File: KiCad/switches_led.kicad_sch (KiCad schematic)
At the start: 70 parts, among them Q2 MMBT3904, Q3 MMBT3904, Q4 MMBT3904, Q5 MMBT3904, Q6 MMBT3904, Q7 MMBT3904, Q8 MMBT3904, Q9 MMBT3904, U3 CD4017BE

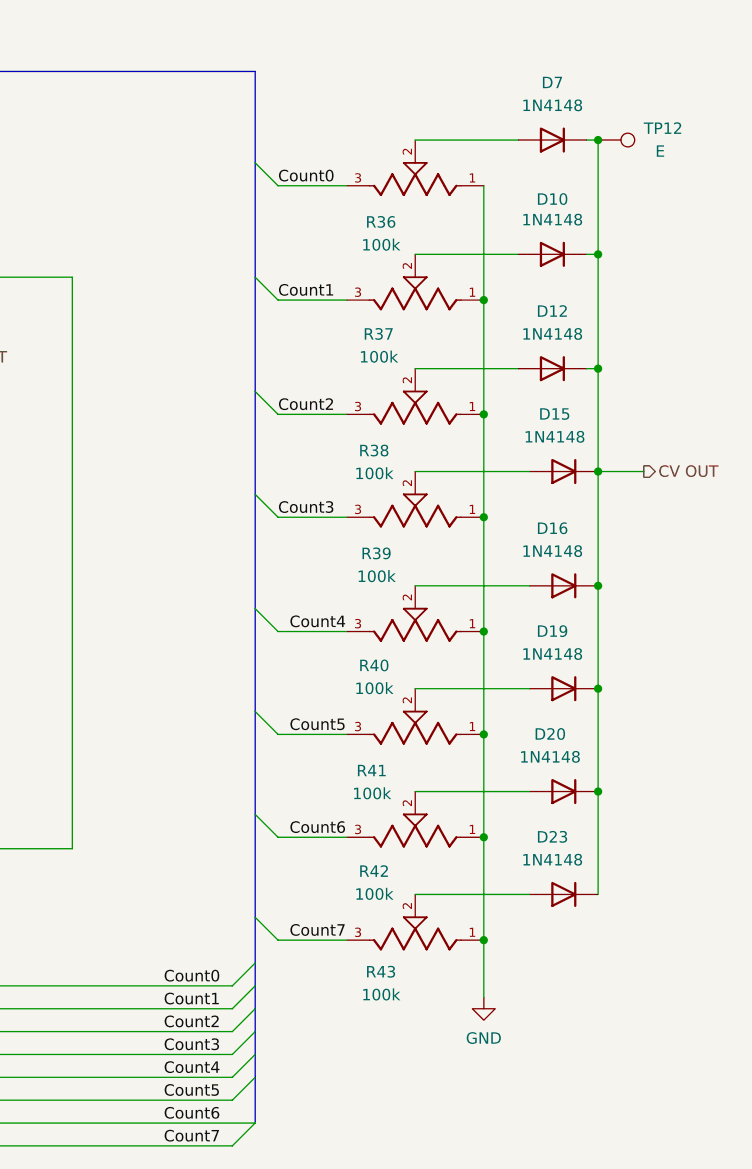
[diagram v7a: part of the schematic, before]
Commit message: fixing drc errors; mirroring potentiometers in sch due to error; mirroring switches on pcb
to do: change symbol description potentiometer (cw, ccw)
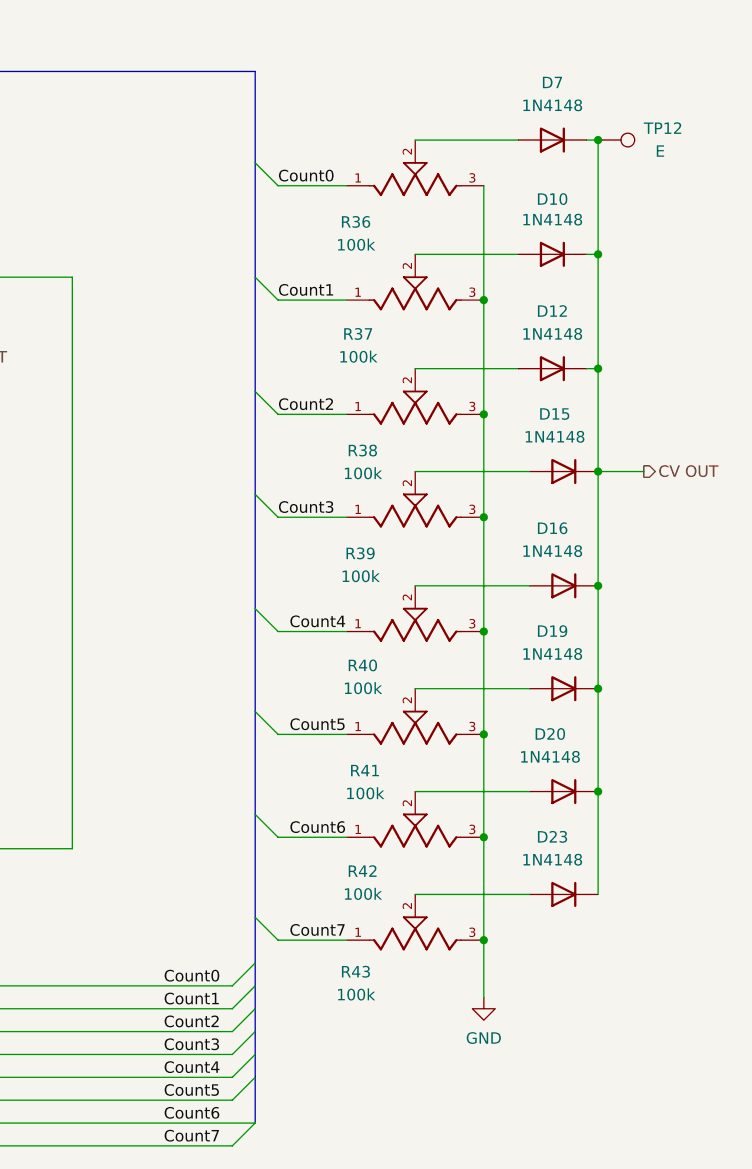
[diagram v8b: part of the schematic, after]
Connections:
- net Count0: now also R36.1; no longer R36.3
- net Count1: now also R37.1; no longer R37.3
- net Count2: now also R38.1; no longer R38.3
- net Count3: now also R39.1; no longer R39.3
- net Count4: now also R40.1; no longer R40.3
- net Count5: now also R41.1; no longer R41.3
- net Count6: now also R42.1; no longer R42.3
- net Count7: now also R43.1; no longer R43.3
- net GND: now also R36.3, R37.3, R38.3, R39.3, R40.3, R41.3, R42.3, R43.3; no longer R36.1, R37.1, R38.1, R39.1, R40.1, R41.1, R42.1, R43.1
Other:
- moved on the sheet: R36, R37, R38, R39, R40, R41, R42, R43
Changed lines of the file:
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@@
 	(symbol
 		(lib_id "Eurorack:Potentiometer_Alpha_RD901F_Vertical")
-		(at 247.65 52.07 180)
+		(at 247.65 52.07 0)
+		(mirror x)
 		(unit 1)
 		(exclude_from_sim no)
@@
 		(dnp no)
 		(property "Reference" "R37"
-			(at 243.586 55.88 0)
+			(at 241.3 55.88 0)
 			(effects
 				(font
@@
 		)
 		(property "Value" "100k"
-			(at 243.586 58.42 0)
+			(at 241.3 58.42 0)
 			(effects
 				(font
@@
 	(symbol
 		(lib_id "Eurorack:Potentiometer_Alpha_RD901F_Vertical")
-		(at 247.65 123.19 180)
+		(at 247.65 123.19 0)
+		(mirror x)
 		(unit 1)
 		(exclude_from_sim no)
@@
 		(dnp no)
 		(property "Reference" "R43"
-			(at 243.84 126.746 0)
+			(at 241.046 126.746 0)
 			(effects
 				(font
@@
 		)
 		(property "Value" "100k"
-			(at 243.84 129.286 0)
+			(at 241.046 129.286 0)
 			(effects
 				(font
@@
 	(symbol
 		(lib_id "Eurorack:Potentiometer_Alpha_RD901F_Vertical")
-		(at 247.65 76.2 180)
+		(at 247.65 76.2 0)
+		(mirror x)
 		(unit 1)
 		(exclude_from_sim no)
@@
 		(dnp no)
 		(property "Reference" "R39"
-			(at 243.332 80.264 0)
+			(at 241.554 80.264 0)
 			(effects
 				(font
@@
 		)
 		(property "Value" "100k"
-			(at 243.332 82.804 0)
+			(at 241.554 82.804 0)
 			(effects
 				(font
@@
 	(symbol
 		(lib_id "Eurorack:Potentiometer_Alpha_RD901F_Vertical")
-		(at 247.65 64.77 180)
+		(at 247.65 64.77 0)
+		(mirror x)
 		(unit 1)
 		(exclude_from_sim no)
@@
 		(dnp no)
 		(property "Reference" "R38"
-			(at 243.078 68.834 0)
+			(at 241.808 68.834 0)
 			(effects
 				(font
@@
 		)
 		(property "Value" "100k"
-			(at 243.078 71.374 0)
+			(at 241.808 71.374 0)
 			(effects
 				(font
@@
 	(symbol
 		(lib_id "Eurorack:Potentiometer_Alpha_RD901F_Vertical")
-		(at 247.65 88.9 180)
+		(at 247.65 88.9 0)
+		(mirror x)
 		(unit 1)
 		(exclude_from_sim no)
@@
 		(dnp no)
 		(property "Reference" "R40"
-			(at 243.078 92.71 0)
+			(at 241.808 92.71 0)
 			(effects
 				(font
@@
 		)
 		(property "Value" "100k"
-			(at 243.078 95.25 0)
+			(at 241.808 95.25 0)
 			(effects
 				(font
@@
 	(symbol
 		(lib_id "Eurorack:Potentiometer_Alpha_RD901F_Vertical")
-		(at 247.65 39.37 180)
+		(at 247.65 39.37 0)
+		(mirror x)
 		(unit 1)
 		(exclude_from_sim no)
@@
 		(dnp no)
 		(property "Reference" "R36"
-			(at 243.84 43.434 0)
+			(at 241.046 43.434 0)
 			(effects
 				(font
@@
 		)
 		(property "Value" "100k"
-			(at 243.84 45.974 0)
+			(at 241.046 45.974 0)
 			(effects
 				(font
@@
 	(symbol
 		(lib_id "Eurorack:Potentiometer_Alpha_RD901F_Vertical")
-		(at 247.65 100.33 180)
+		(at 247.65 100.33 0)
+		(mirror x)
 		(unit 1)
 		(exclude_from_sim no)
@@
 		(dnp no)
 		(property "Reference" "R41"
-			(at 242.824 104.394 0)
+			(at 242.062 104.394 0)
 			(effects
 				(font
@@
 		)
 		(property "Value" "100k"
-			(at 242.824 106.934 0)
+			(at 242.062 106.934 0)
 			(effects
 				(font
@@
 	(symbol
 		(lib_id "Eurorack:Potentiometer_Alpha_RD901F_Vertical")
-		(at 247.65 111.76 180)
+		(at 247.65 111.76 0)
+		(mirror x)
 		(unit 1)
 		(exclude_from_sim no)
@@
 		(dnp no)
 		(property "Reference" "R42"
-			(at 243.078 115.57 0)
+			(at 241.808 115.57 0)
 			(effects
 				(font
@@
 		)
 		(property "Value" "100k"
-			(at 243.078 118.11 0)
+			(at 241.808 118.11 0)
 			(effects
 				(font
